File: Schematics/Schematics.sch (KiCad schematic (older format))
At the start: 12 parts

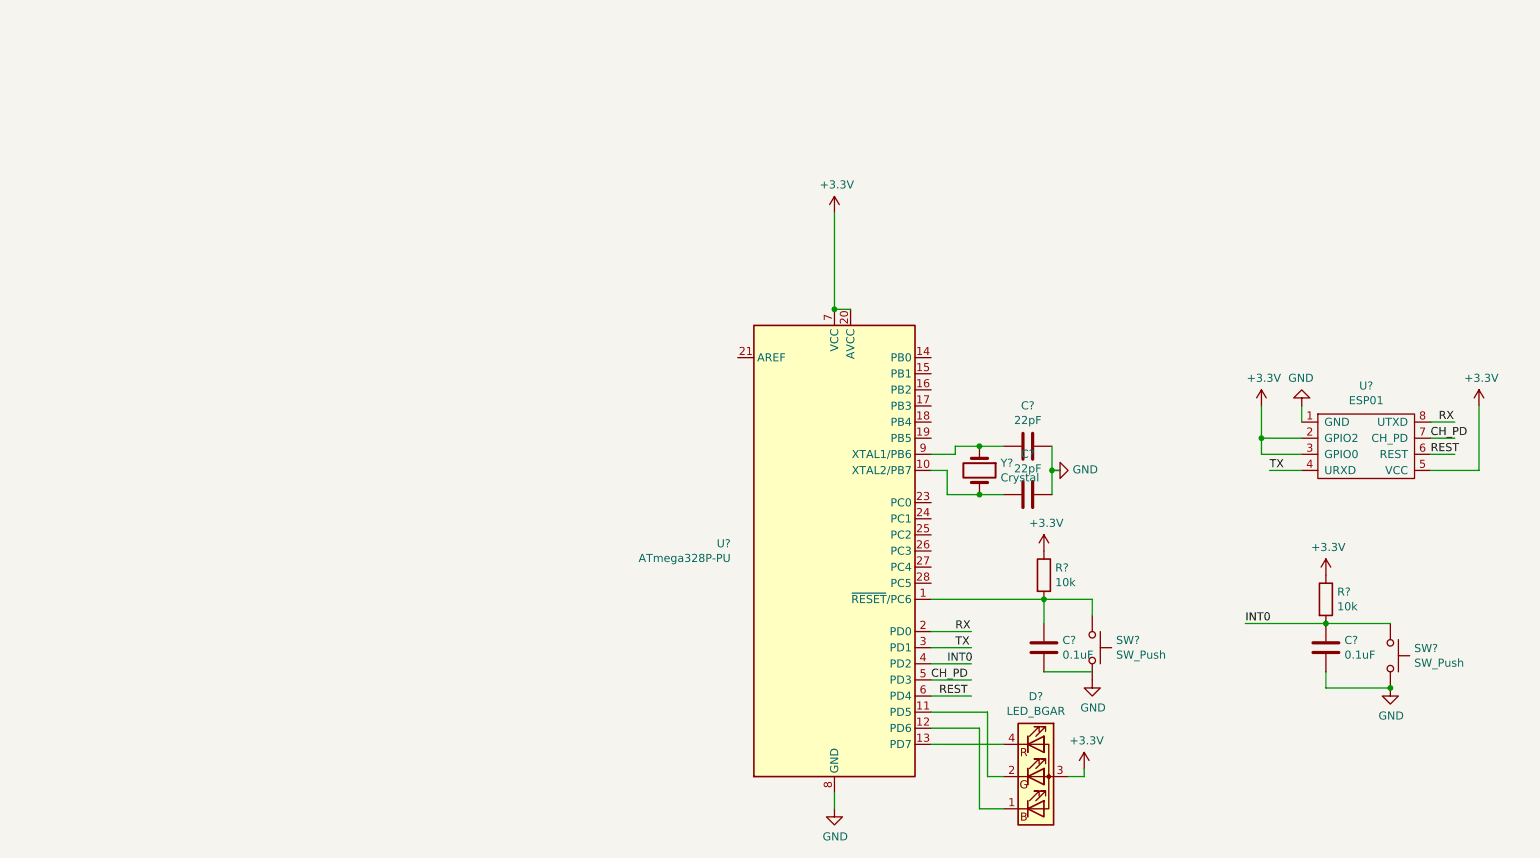
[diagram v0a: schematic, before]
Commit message: The schematics were altered. A Circuit board layout was added.
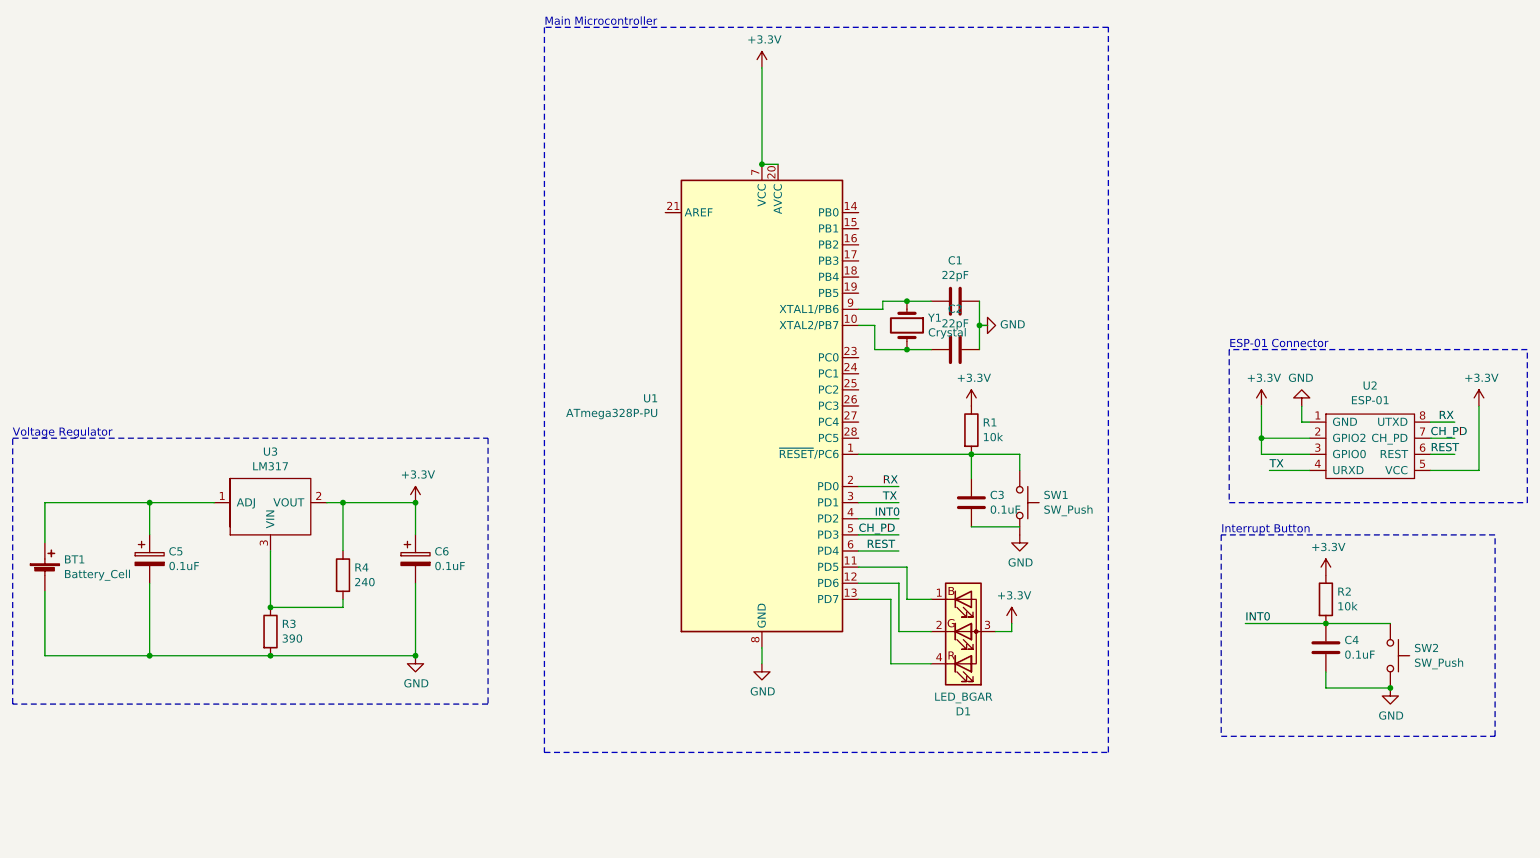
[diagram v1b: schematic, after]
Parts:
- removed U?: ESP01, symbol New_Library:ESP01
- added BT1: Battery_Cell, Laundry_Pulse_Lib:Connector_Battery, symbol Device:Battery_Cell
- added C5, C6: 0.1uF, Capacitor_THT:CP_Radial_D5.0mm_P2.50mm, symbol Device:CP
- added R3: 390, Resistor_THT:R_Axial_DIN0204_L3.6mm_D1.6mm_P2.54mm_Vertical, symbol Device:R
- added R4: 240, Resistor_THT:R_Axial_DIN0204_L3.6mm_D1.6mm_P2.54mm_Vertical, symbol Device:R
- added U2: ESP-01, Laundry_Pulse_Lib:ESP01_Footprint, symbol Laundry_Pulse_Lib:ESP-01
- added U3: LM317, Laundry_Pulse_Lib:LM317_Custom, symbol Laundry_Pulse_Lib:LM317
- C1, C2: renamed from C?; footprint (none) -> Capacitor_THT:C_Disc_D4.3mm_W1.9mm_P5.00mm
- C3, C4: renamed from C?; footprint (none) -> Capacitor_THT:C_Disc_D6.0mm_W2.5mm_P5.00mm
- D1: renamed from D?; footprint (none) -> Laundry_Pulse_Lib:Connector_LED
- R1, R2: renamed from R?; footprint (none) -> Resistor_THT:R_Axial_DIN0204_L3.6mm_D1.6mm_P2.54mm_Vertical
- SW1, SW2: renamed from SW?; footprint (none) -> Laundry_Pulse_Lib:Connector_Button
- Y1: renamed from Y?; footprint (none) -> Crystal:Crystal_HC18-U_Vertical
- gave numbers to parts that had none: 1
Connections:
- wire segments 48 -> 68
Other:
- note added: "ESP-01 Connector"
- note added: "Interrupt Button"
- note added: "Main Microcontroller"
- note added: "Voltage Regulator"
- moved on the sheet: C1, C2, C3, D1, R1, SW1, U1, Y1
